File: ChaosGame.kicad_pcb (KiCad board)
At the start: 4 copper layers, 88.9 x 50.8 mm, 81 parts, among them J1 USB_OTG, J5 RNG, Q1 2N3904, Q2 2N3904, U1 TLE2426, U10 74HC74, U11 74HC74, U12 74HC74, U13 74HC74, U2 TLV271, U3 LM311, U4 74HC74, U5 INA826, U6 TLV272, U7 4066, U8 TLV272, U9 74HC14

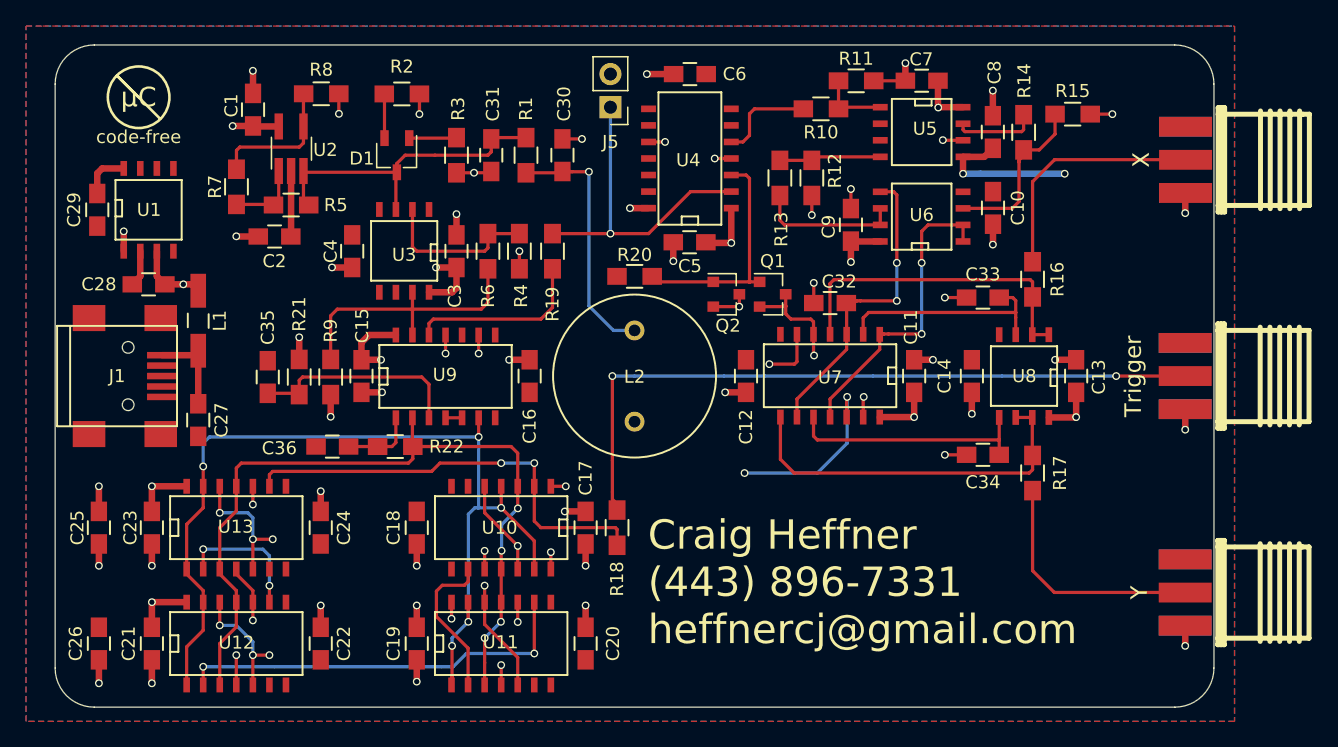
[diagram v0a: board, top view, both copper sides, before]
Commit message: Renamed files to ChaosGame; implemented some changes from master.
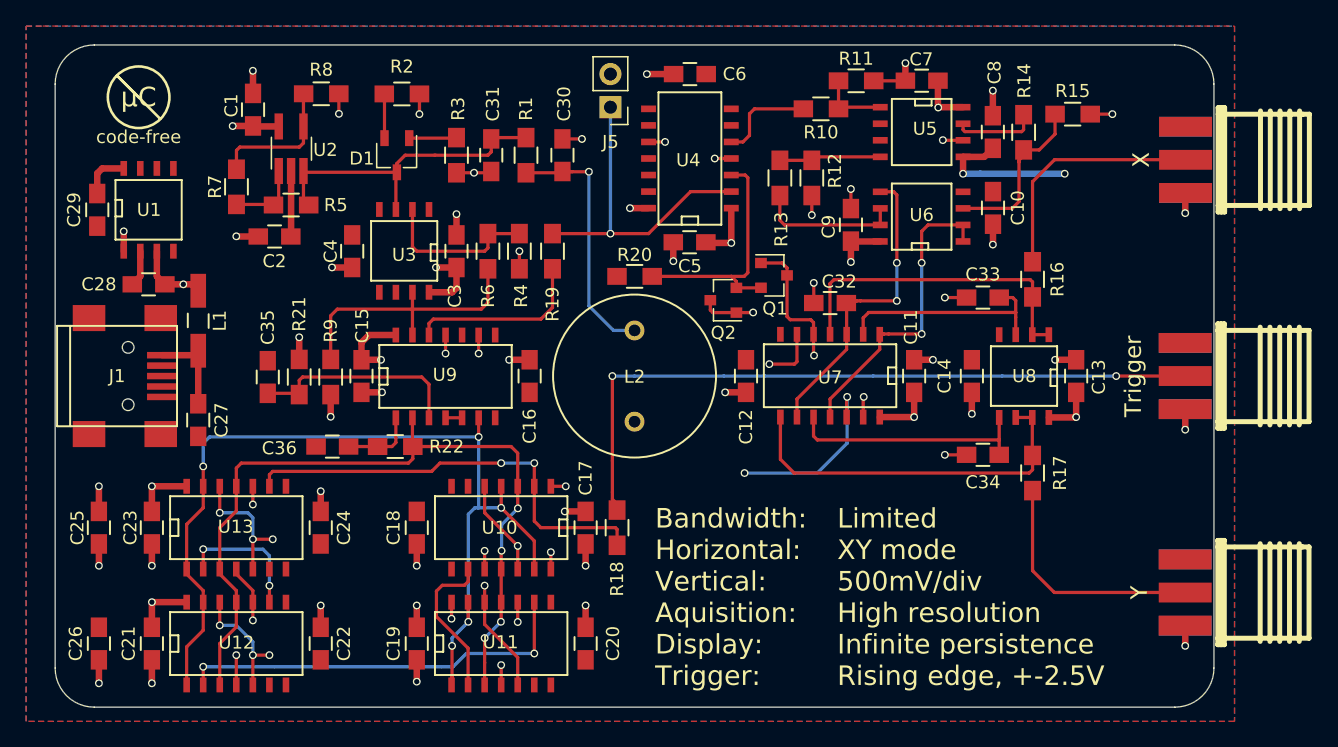
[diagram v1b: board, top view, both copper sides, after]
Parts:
- moved Q1 1.45 mm to (160.2, 89.0)
- moved Q2 0.51 mm to (156.4, 90.9), turned to 180 degrees
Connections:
- Q1 pad 1: Net-(Q1-Pad1) -> CLOCK_CYCLE_0
- Q1 pad 2: CLOCK_CYCLE_0 -> Net-(Q1-Pad2)
- Q2 pad 1: Net-(Q1-Pad1) -> CLOCK_CYCLE_2
- Q2 pad 2: CLOCK_CYCLE_2 -> Net-(Q1-Pad2)
- R20 pad 1: Net-(Q1-Pad1) -> Net-(Q1-Pad2)
- U4 pad 3: Net-(Q1-Pad1) -> Net-(Q1-Pad2)
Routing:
- net Net-(Q1-Pad2): track 0.00 -> 19.6 mm
- net Net-(Q1-Pad1): track 18.0 -> 0.00 mm
- net CLOCK_CYCLE_0: track 52.0 -> 53.9 mm
- net (no net): track 0.00 -> 1.29 mm
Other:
- board text added: "0.506127"
- board text added: "Bandwidth: Horizontal: Vertical: Aquisition: Display: Trigger:"
- board text added: "Limited XY mode 500mV/div High resolution Infinite persistence Rising edge, +-2.5V"
- board text removed: "Craig Heffner (443) 896-7331 heffnercj@gmail.com"
- board text removed: "http://www.analogzoo.com/businesscard"

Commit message: Final updates to PCB and schematics.
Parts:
- R13: value 10k -> 15k
- R14: value 10k -> 0
- moved R15 1.55 mm to (181.7, 77.2), turned to 90 degrees
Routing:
- net Net-(R14-Pad2): track 13.2 -> 11.5 mm
- net Net-(U6-Pad1): track 23.7 -> 22.3 mm
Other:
- board text added: "http://www.analogzoo.com"
